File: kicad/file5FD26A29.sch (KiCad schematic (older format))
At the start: 7 parts, among them J2 6339191-4, T1 H1102NL, U3 LAN8742A-CZ-TR, U4 USBLC6-4SC6

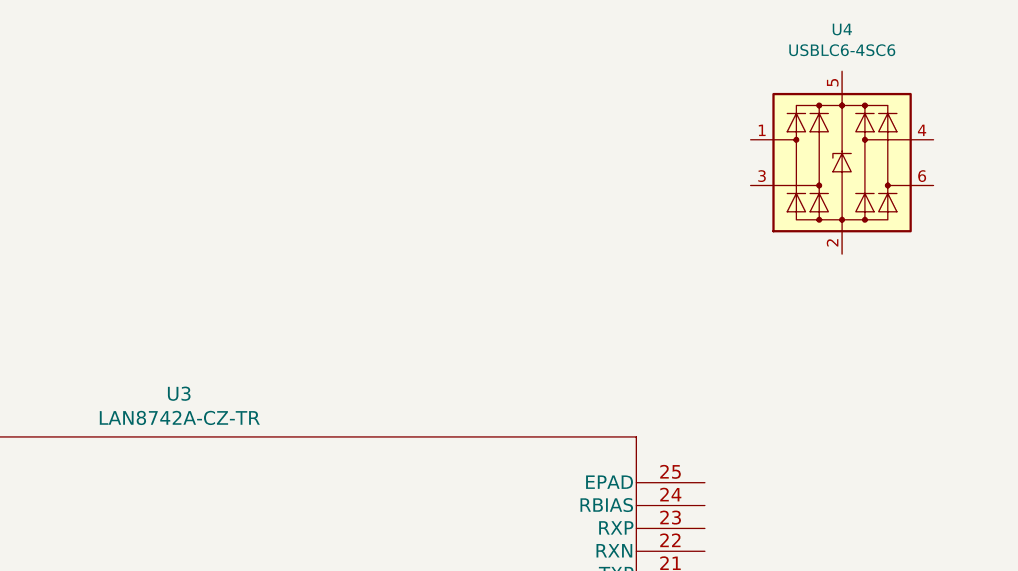
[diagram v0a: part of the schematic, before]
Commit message: Power reg U2/U3 and supporting components
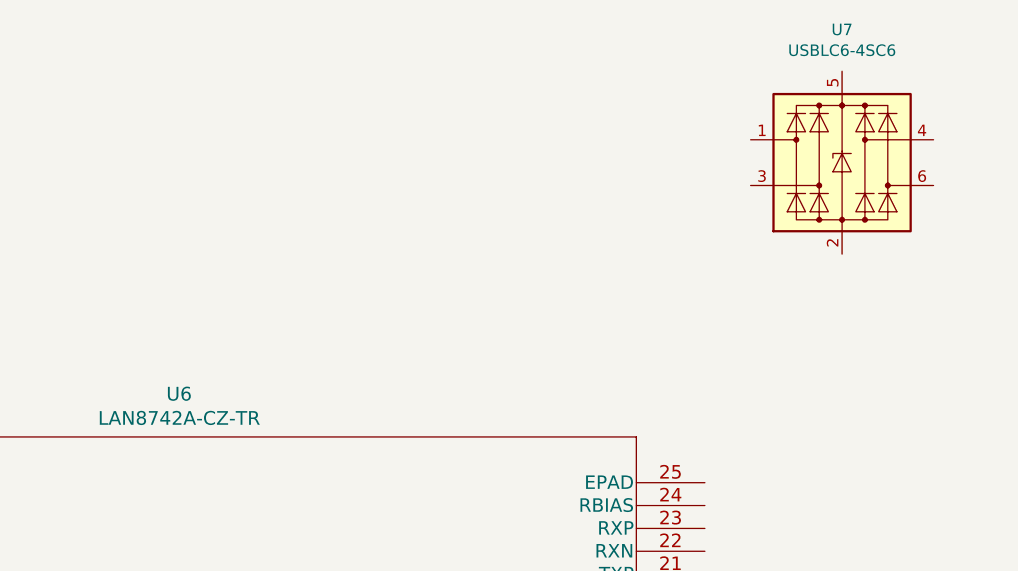
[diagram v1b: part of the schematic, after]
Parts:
- renumbered U4 to U7
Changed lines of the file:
@@
 P 2650 5050
 AR Path="/5FD274C1" Ref="U3"  Part="1"
-AR Path="/5FD26A2A/5FD274C1" Ref="U3"  Part="1"
-F 0 "U3" H 4950 5437 60  0000 C CNN
+AR Path="/5FD26A2A/5FD274C1" Ref="U6"  Part="1"
+F 0 "U6" H 4950 5437 60  0000 C CNN
 F 1 "LAN8742A-CZ-TR" H 4950 5331 60  0000 C CNN
 F 2 "SQFN24_4X4MC_MCH" H 4950 5290 60  0001 C CNN
@@
 $EndComp
 $Comp
-L Power_Protection:USBLC6-4SC6 U4
+L Power_Protection:USBLC6-4SC6 U7
 U 1 1 5FD2935E
 P 7850 3650
-F 0 "U4" H 7850 4231 50  0000 C CNN
+F 0 "U7" H 7850 4231 50  0000 C CNN
 F 1 "USBLC6-4SC6" H 7850 4140 50  0000 C CNN
 F 2 "Package_TO_SOT_SMD:SOT-23-6" H 7850 3150 50  0001 C CNN

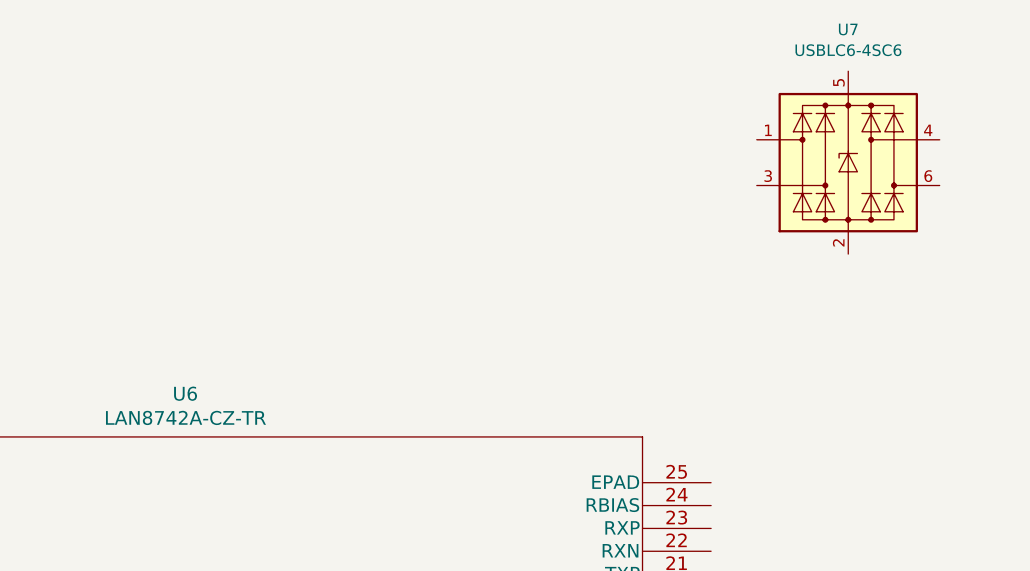
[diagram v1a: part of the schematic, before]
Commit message: Power reg Section 1 initial entry; annotate
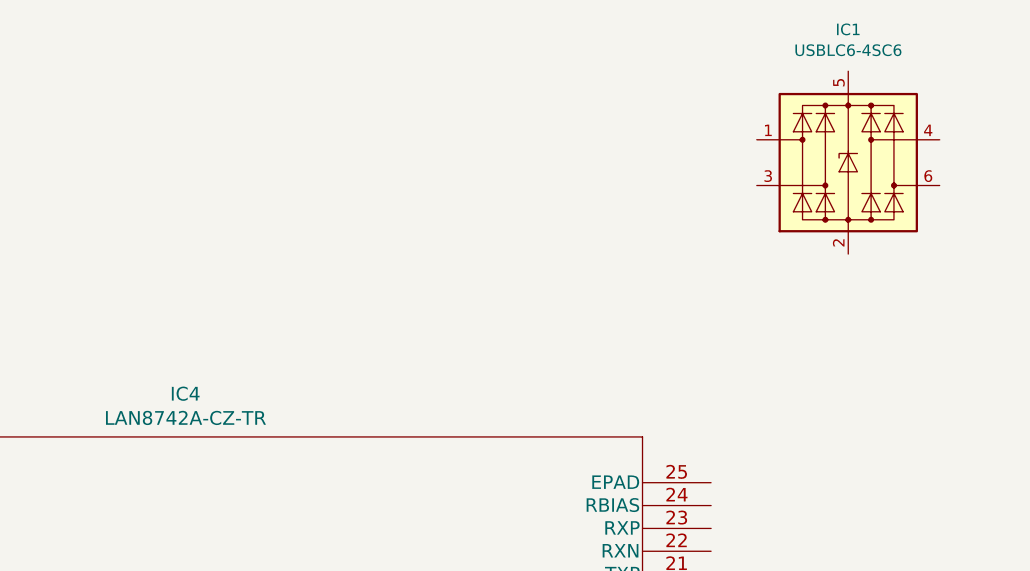
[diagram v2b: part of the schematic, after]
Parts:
- renumbered U7 to IC1
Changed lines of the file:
@@
 P 2650 5050
 AR Path="/5FD274C1" Ref="U3"  Part="1"
-AR Path="/5FD26A2A/5FD274C1" Ref="U6"  Part="1"
-F 0 "U6" H 4950 5437 60  0000 C CNN
+AR Path="/5FD26A2A/5FD274C1" Ref="IC4"  Part="1"
+F 0 "IC4" H 4950 5437 60  0000 C CNN
 F 1 "LAN8742A-CZ-TR" H 4950 5331 60  0000 C CNN
 F 2 "SQFN24_4X4MC_MCH" H 4950 5290 60  0001 C CNN
@@
 $EndComp
 $Comp
-L Power_Protection:USBLC6-4SC6 U7
+L Power_Protection:USBLC6-4SC6 IC1
 U 1 1 5FD2935E
 P 7850 3650
-F 0 "U7" H 7850 4231 50  0000 C CNN
+F 0 "IC1" H 7850 4231 50  0000 C CNN
 F 1 "USBLC6-4SC6" H 7850 4140 50  0000 C CNN
 F 2 "Package_TO_SOT_SMD:SOT-23-6" H 7850 3150 50  0001 C CNN

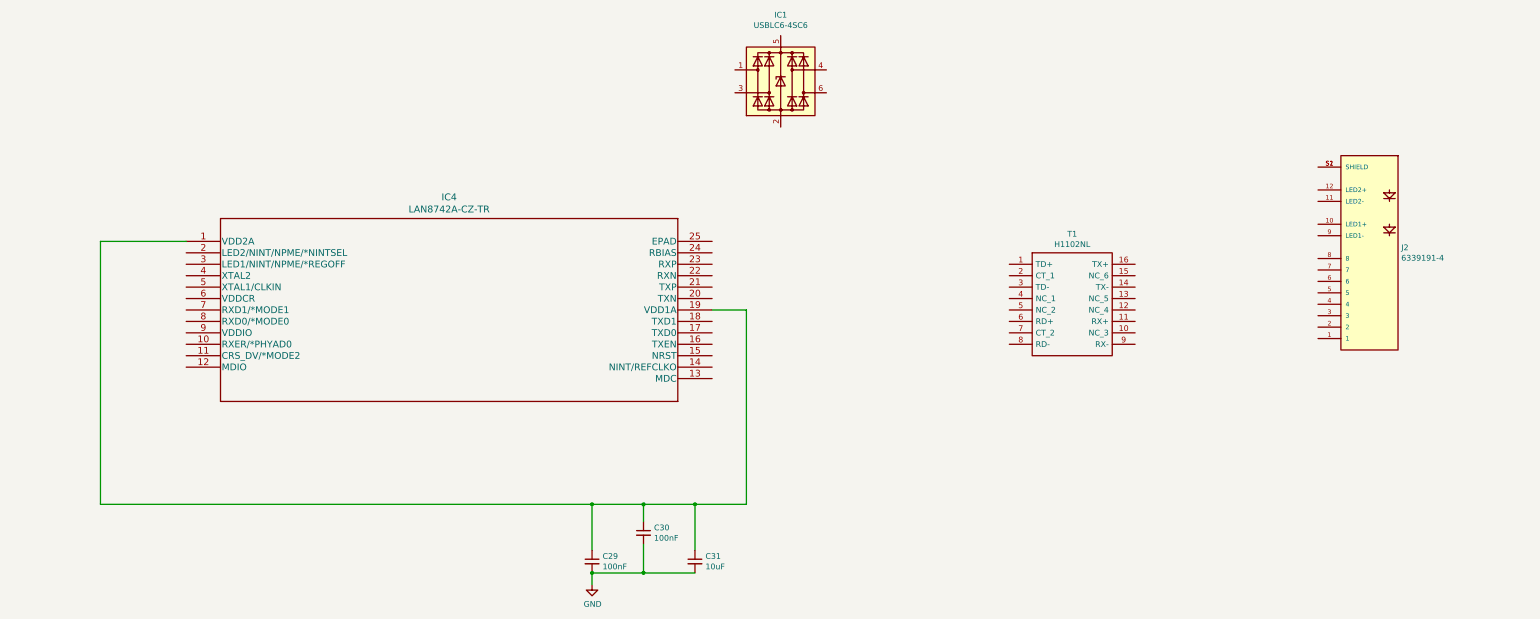
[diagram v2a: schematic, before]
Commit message: Voltage control for regulator; work on Ethernet
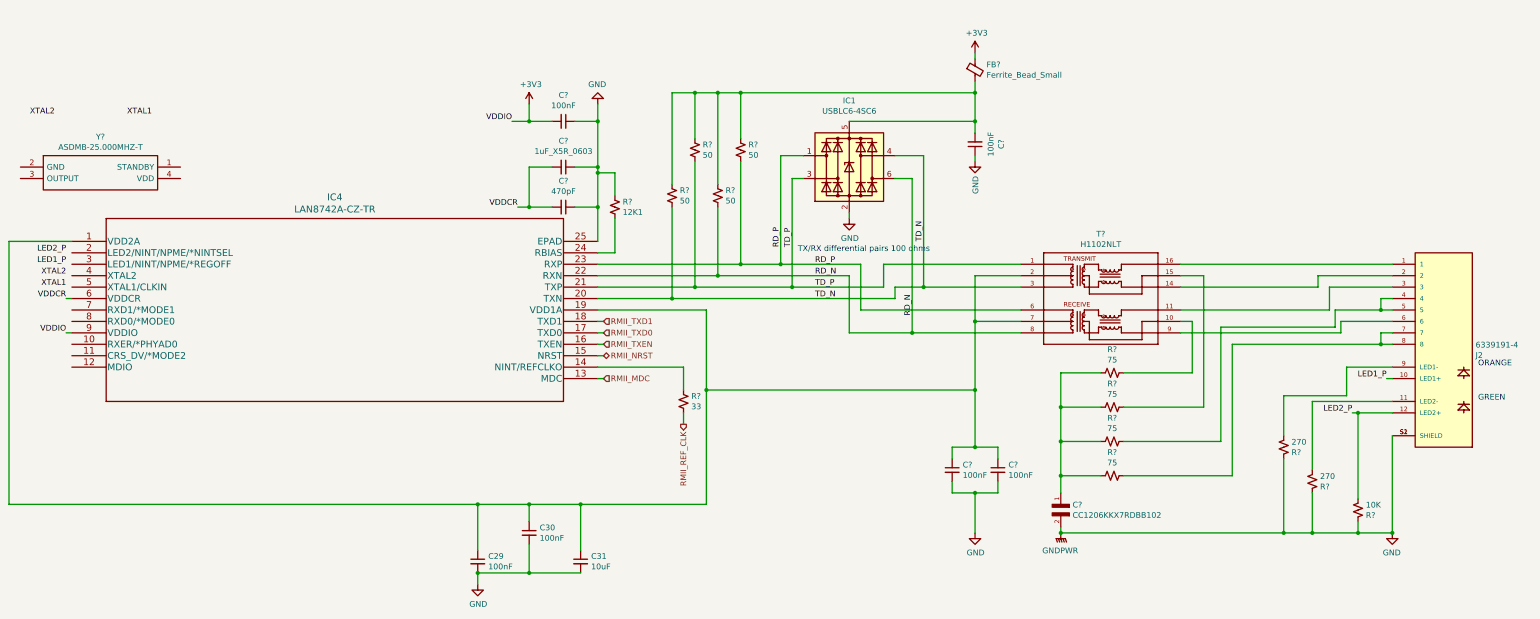
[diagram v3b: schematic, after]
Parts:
- removed T1: H1102NL, SOIC127P940X597-16N, symbol H1102NL:H1102NL
- added C? (x4): 100nF, symbol Device:C_Small
- added C?: 470pF, symbol Device:C_Small
- added C?: 1uF_X5R_0603, symbol Device:C_Small
- added C?: CC1206KKX7RDBB102, CAPC3216X95N, symbol CC1206KKX7RDBB102:CC1206KKX7RDBB102
- added FB?: Ferrite_Bead_Small, symbol Device:Ferrite_Bead_Small
- added R? (x4): 50, symbol Device:R_Small_US
- added R?: 12K1, symbol Device:R_Small_US
- added R?: 33, symbol Device:R_Small_US
- added R? (x2): 270, symbol Device:R_Small_US
- added R?: 10K, symbol Device:R_Small_US
- added R? (x4): 75, symbol Device:R_Small_US
- added T?: H1102NLT, XFMR_H1102NLT, symbol H1102NLT:H1102NLT
- added Y?: ASDMB-25.000MHZ-T, ASDMB25000MHZT, symbol SamacSys_Parts:ASDMB-25.000MHZ-T
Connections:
- net GND: now also IC1.2 (GND), J2.S1 (SHIELD), J2.S2 (SHIELD), U3.25 (EPAD), C?.1, C?.1, C?.1, C?.1, C?.2, C?.2, C?.2, R?.1, R?.1, R?.1, R?.1
- net at C29.1, C30.1, C31.1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: now also C?.1, C?.1, T?.2, T?.7
- net RMII_MDC: now reaches U3.13 (MDC)
- net at U3.14 (NINT/REFCLKO): now also R?.1
- net RMII_NRST: now reaches U3.15 (NRST)
- net RMII_TXEN: now reaches U3.16 (TXEN)
- net RMII_TXD0: now reaches U3.17 (TXD0)
- net RMII_TXD1: now reaches U3.18 (TXD1)
- net TD_N: now reaches U3.20 (TXN)
- net TD_N: now also IC1.4 (I/O3), R?.2, T?.3
- net TD_P: now reaches U3.21 (TXP)
- net TD_P: now also IC1.3 (I/O2), R?.2, T?.1
- net RD_N: now reaches U3.22 (RXN)
- net RD_N: now also IC1.6 (I/O4), R?.2, T?.8
- net RD_P: now reaches U3.23 (RXP)
- net RD_P: now also IC1.1 (I/O1), R?.2, T?.6
- net at U3.24 (RBIAS): now also R?.2
- net VDDCR: now reaches U3.6 (VDDCR)
- net VDDCR: now also C?.2, C?.2
- net +3V3: now reaches U3.9 (VDDIO)
- net +3V3: now also C?.2, FB?.1
- net at IC1.5 (VBUS): now also C?.2, FB?.2, R?.1, R?.1, R?.1, R?.1
- net at J2.1: now also T?.16
- net LED1_P: now reaches J2.10 (LED1+)
- net at J2.11 (LED2-): now also R?.2
- net LED2_P: now reaches J2.12 (LED2+)
- net LED2_P: now also R?.2
- net at J2.2: now also T?.14
- net at J2.3: now also T?.11
- net at J2.4: now also J2.5, R?.1
- net at J2.6: now also T?.9
- net at J2.7: now also J2.8, R?.1
- net at J2.9 (LED1-): now also R?.2
- new net: R?.1, T?.10
- new net: R?.1, T?.15
- new net: C?.1, R?.2, R?.2, R?.2, R?.2
- new net RMII_REF_CLK: R?.2
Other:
- note added: "GREEN"
- note added: "ORANGE"
- note added: "TX/RX differential pairs 100 ohms"
- moved on the sheet: C29, C30, C31, IC1, IC4, J2

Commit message: Ethernet initial schematic; start ERC
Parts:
- removed Y?: ASDMB-25.000MHZ-T, ASDMB25000MHZT, symbol SamacSys_Parts:ASDMB-25.000MHZ-T
- added R41, R45, R46, R47: 10K, symbol Device:R_Small_US
- added R42, R43, R44: 33, symbol Device:R_Small_US
- added R48: 1K5, symbol Device:R_Small_US
- added Y2: SXT3249AA17-25.000M, SXT32420BA48, symbol SamacSys_Parts:SXT32420BA48
- gave numbers to parts that had none: 22
- renumbered IC1 to IC3
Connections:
- net +3V3: now also R45.1, R46.1, R47.1, R48.2
- net GND: now also R41.2, Y2.2 (GND_1), Y2.4 (GND_2)
- net LED1_P: now also U3.3 (LED1/NINT/NPME/*REGOFF)
- net LED2_P: now also U3.2 (LED2/NINT/NPME/*NINTSEL)
- net XTAL1: now also U3.5 (XTAL1/CLKIN), Y2.1 (CRYSTAL_1)
- net XTAL2: now also U3.4 (XTAL2), Y2.3 (CRYSTAL_2)
- net at U3.10 (RXER/*PHYAD0): now also R41.1
- net at U3.11 (CRS_DV/*MODE2): now also R42.1, R47.2
- net RMII_MDIO: now reaches U3.12 (MDIO)
- net RMII_MDIO: now also R48.1
- net at U3.7 (RXD1/*MODE1): now also R43.1, R45.2
- net at U3.8 (RXD0/*MODE0): now also R44.1, R46.2
- new net RMII_CRS_DV: R42.2
- new net RMII_RXD0: R44.2
- new net RMII_RXD1: R43.2
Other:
- moved on the sheet: C29, C30, C31, C83, C84, C85, C86, C87, C88, C89, FB1, IC2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
